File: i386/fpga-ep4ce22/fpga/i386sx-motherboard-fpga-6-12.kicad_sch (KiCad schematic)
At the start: 1 part, among them U16 SN74LVC8T245PWR

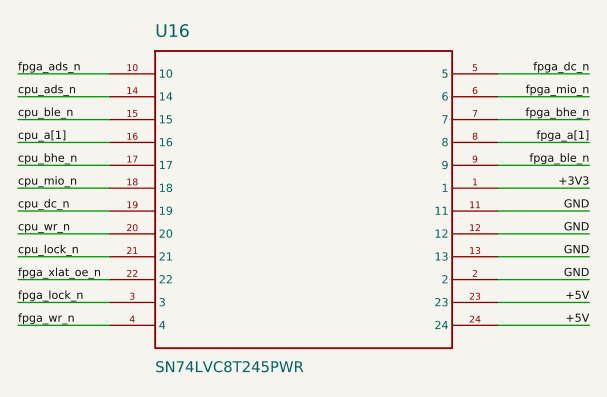
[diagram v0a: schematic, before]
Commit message: Publish the motherboards' KiCad files
From socket3@c0f6464 socket7@9205469 socket370@524f5b1 i386@bea926c
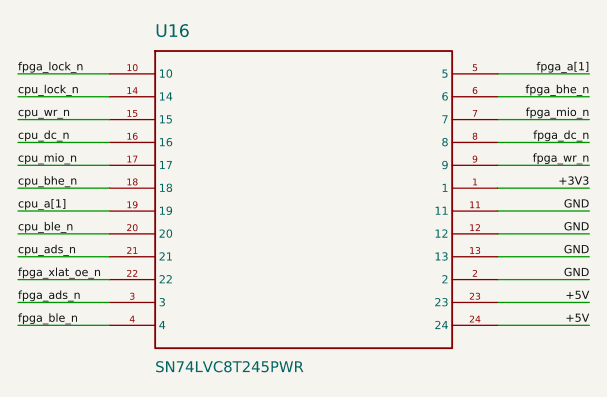
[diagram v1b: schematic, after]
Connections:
- net cpu_a[1]: now also U16.19; no longer U16.16
- net cpu_ads_n: now also U16.21; no longer U16.14
- net cpu_bhe_n: now also U16.18; no longer U16.17
- net cpu_ble_n: now also U16.20; no longer U16.15
- net cpu_dc_n: now also U16.16; no longer U16.19
- net cpu_lock_n: now also U16.14; no longer U16.21
- net cpu_mio_n: now also U16.17; no longer U16.18
- net cpu_wr_n: now also U16.15; no longer U16.20
- net fpga_a[1]: now also U16.5; no longer U16.8
- net fpga_ads_n: now also U16.3; no longer U16.10
- net fpga_bhe_n: now also U16.6; no longer U16.7
- net fpga_ble_n: now also U16.4; no longer U16.9
- net fpga_dc_n: now also U16.8; no longer U16.5
- net fpga_lock_n: now also U16.10; no longer U16.3
- net fpga_mio_n: now also U16.7; no longer U16.6
- net fpga_wr_n: now also U16.9; no longer U16.4
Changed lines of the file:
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@@
     (property "Reference" "U16" (at 44.46 17.65 0) (effects (font (size 1.4 1.4)) (justify left bottom)))
     (property "Value" "SN74LVC8T245PWR" (at 44.46 53.47 0) (effects (font (size 1.2 1.2)) (justify left top)))
-    (instances (project "i386sx-motherboard" (path "/0ac398a9-1d89-4090-a36f-db7b4d3d6c0d/5d30386c-054a-400c-917f-4f6456db81bb" (reference "U16") (unit 1))))
+    (instances (project "i386sx-motherboard" (path "/ea05416d-ce24-4c39-9113-85b33d9a88b0/f592cd23-5685-4f67-8d99-dd0dd90f61dd" (reference "U16") (unit 1))))
   )
   (wire (pts (xy 39.38 21.59) (xy 29.22 21.59)) (stroke (width 0) (type default)))
@@
   (wire (pts (xy 82.54 46.99) (xy 92.70 46.99)) (stroke (width 0) (type default)))
   (wire (pts (xy 82.54 49.53) (xy 92.70 49.53)) (stroke (width 0) (type default)))
-  (label "fpga_ads_n" (at 29.22 21.59 0) (effects (font (size 0.9 0.9)) (justify left bottom)))
-  (label "cpu_ads_n" (at 29.22 24.13 0) (effects (font (size 0.9 0.9)) (justify left bottom)))
-  (label "cpu_ble_n" (at 29.22 26.67 0) (effects (font (size 0.9 0.9)) (justify left bottom)))
-  (label "cpu_a[1]" (at 29.22 29.21 0) (effects (font (size 0.9 0.9)) (justify left bottom)))
-  (label "cpu_bhe_n" (at 29.22 31.75 0) (effects (font (size 0.9 0.9)) (justify left bottom)))
-  (label "cpu_mio_n" (at 29.22 34.29 0) (effects (font (size 0.9 0.9)) (justify left bottom)))
-  (label "cpu_dc_n" (at 29.22 36.83 0) (effects (font (size 0.9 0.9)) (justify left bottom)))
-  (label "cpu_wr_n" (at 29.22 39.37 0) (effects (font (size 0.9 0.9)) (justify left bottom)))
-  (label "cpu_lock_n" (at 29.22 41.91 0) (effects (font (size 0.9 0.9)) (justify left bottom)))
+  (label "fpga_lock_n" (at 29.22 21.59 0) (effects (font (size 0.9 0.9)) (justify left bottom)))
+  (label "cpu_lock_n" (at 29.22 24.13 0) (effects (font (size 0.9 0.9)) (justify left bottom)))
+  (label "cpu_wr_n" (at 29.22 26.67 0) (effects (font (size 0.9 0.9)) (justify left bottom)))
+  (label "cpu_dc_n" (at 29.22 29.21 0) (effects (font (size 0.9 0.9)) (justify left bottom)))
+  (label "cpu_mio_n" (at 29.22 31.75 0) (effects (font (size 0.9 0.9)) (justify left bottom)))
+  (label "cpu_bhe_n" (at 29.22 34.29 0) (effects (font (size 0.9 0.9)) (justify left bottom)))
+  (label "cpu_a[1]" (at 29.22 36.83 0) (effects (font (size 0.9 0.9)) (justify left bottom)))
+  (label "cpu_ble_n" (at 29.22 39.37 0) (effects (font (size 0.9 0.9)) (justify left bottom)))
+  (label "cpu_ads_n" (at 29.22 41.91 0) (effects (font (size 0.9 0.9)) (justify left bottom)))
   (label "fpga_xlat_oe_n" (at 29.22 44.45 0) (effects (font (size 0.9 0.9)) (justify left bottom)))
-  (label "fpga_lock_n" (at 29.22 46.99 0) (effects (font (size 0.9 0.9)) (justify left bottom)))
-  (label "fpga_wr_n" (at 29.22 49.53 0) (effects (font (size 0.9 0.9)) (justify left bottom)))
-  (label "fpga_dc_n" (at 92.70 21.59 0) (effects (font (size 0.9 0.9)) (justify right bottom)))
-  (label "fpga_mio_n" (at 92.70 24.13 0) (effects (font (size 0.9 0.9)) (justify right bottom)))
-  (label "fpga_bhe_n" (at 92.70 26.67 0) (effects (font (size 0.9 0.9)) (justify right bottom)))
-  (label "fpga_a[1]" (at 92.70 29.21 0) (effects (font (size 0.9 0.9)) (justify right bottom)))
-  (label "fpga_ble_n" (at 92.70 31.75 0) (effects (font (size 0.9 0.9)) (justify right bottom)))
+  (label "fpga_ads_n" (at 29.22 46.99 0) (effects (font (size 0.9 0.9)) (justify left bottom)))
+  (label "fpga_ble_n" (at 29.22 49.53 0) (effects (font (size 0.9 0.9)) (justify left bottom)))
+  (label "fpga_a[1]" (at 92.70 21.59 0) (effects (font (size 0.9 0.9)) (justify right bottom)))
+  (label "fpga_bhe_n" (at 92.70 24.13 0) (effects (font (size 0.9 0.9)) (justify right bottom)))
+  (label "fpga_mio_n" (at 92.70 26.67 0) (effects (font (size 0.9 0.9)) (justify right bottom)))
+  (label "fpga_dc_n" (at 92.70 29.21 0) (effects (font (size 0.9 0.9)) (justify right bottom)))
+  (label "fpga_wr_n" (at 92.70 31.75 0) (effects (font (size 0.9 0.9)) (justify right bottom)))
   (label "+3V3" (at 92.70 34.29 0) (effects (font (size 0.9 0.9)) (justify right bottom)))
   (label "GND" (at 92.70 36.83 0) (effects (font (size 0.9 0.9)) (justify right bottom)))
